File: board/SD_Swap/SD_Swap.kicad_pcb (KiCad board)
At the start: 4 copper layers, 32 x 27 mm, 44 parts, among them J1 USB_C, Q1 Q_Dual_PNP_PNP_E1B1C2E2B2C1, U1 74LVC2G14, U2 RTS5306E, U3 PCB_SD, U4 93AAxxAT, U5 TS3A27518ERTW, U6 SD_SOCKET, U7 AP2127N-3.3, Y1 12MHz

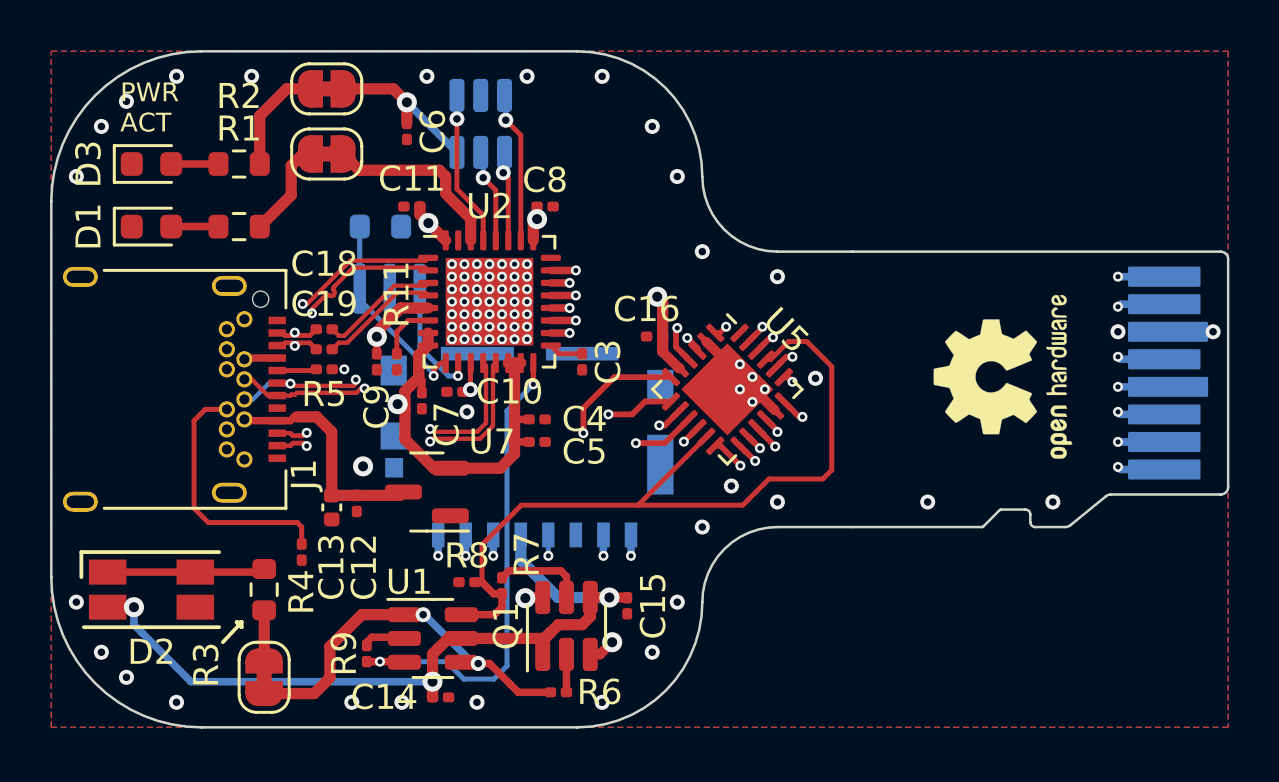
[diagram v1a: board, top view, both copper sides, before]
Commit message: update fix led
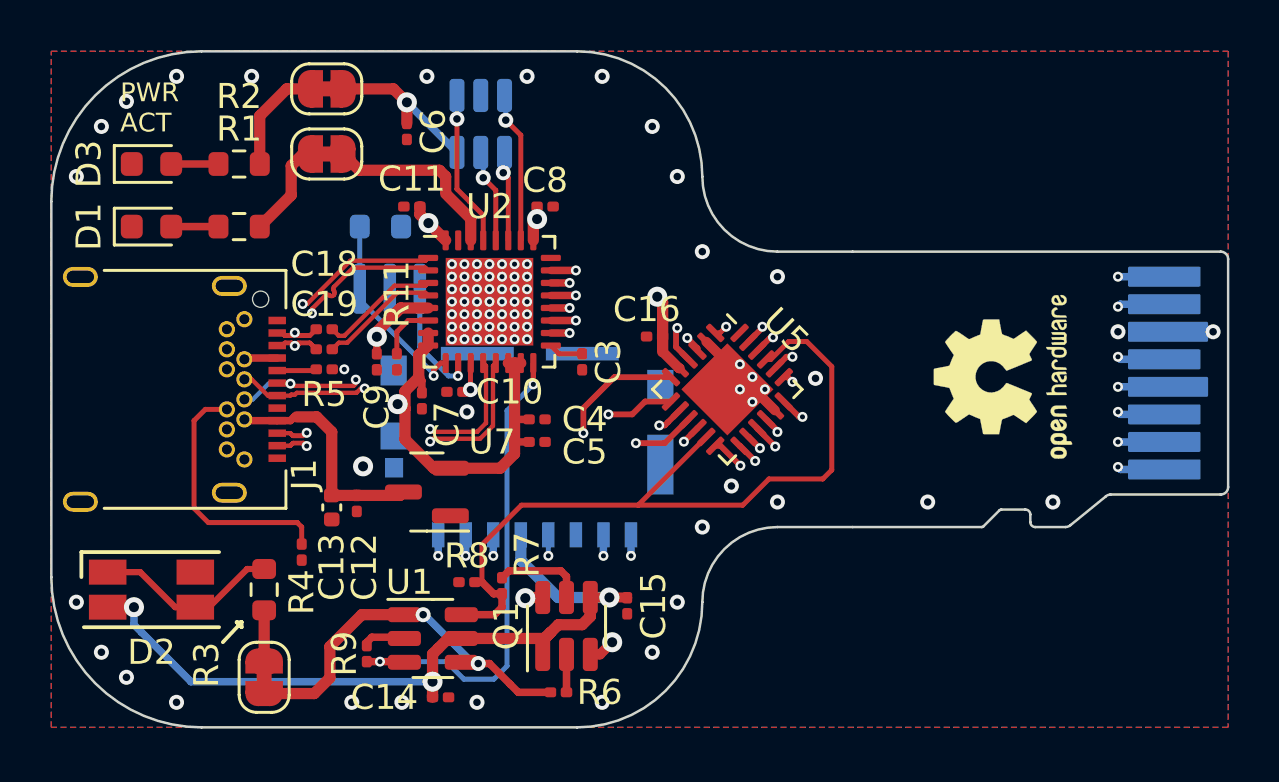
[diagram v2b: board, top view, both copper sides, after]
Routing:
- net Net-(D2-Pad1): track 6.30 -> 7.64 mm
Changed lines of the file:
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@@
     (pad "2" smd rect (at -1.75 0.7 180) (size 1.5 1) (layers "F.Cu" "F.Paste" "F.Mask")
       (net 13 "VCC") (pinfunction "A2") (pintype "input"))
-    (pad "3" smd rect (at 1.75 0.7 180) (size 1.5 1) (layers "F.Cu" "F.Paste" "F.Mask")
+    (pad "3" smd rect (at 1.75 -0.7 180) (size 1.5 1) (layers "F.Cu" "F.Paste" "F.Mask")
       (net 1 "GND") (pinfunction "K1") (pintype "input"))
-    (pad "4" smd rect (at 1.75 -0.7 180) (size 1.5 1) (layers "F.Cu" "F.Paste" "F.Mask")
+    (pad "4" smd rect (at 1.75 0.7 180) (size 1.5 1) (layers "F.Cu" "F.Paste" "F.Mask")
       (net 14 "Net-(D2-Pad1)") (pinfunction "K2") (pintype "input"))
     (model "${KICAD6_3DMODEL_DIR}/LED_SMD.3dshapes/LED_RGB_1210.wrl"
@@
     (fp_line (start 6.9 10.3) (end 5.94 10.3) (layer "Edge.Cuts") (width 0.1))
     (fp_line (start 10.11 9.78) (end 8.71 10.919641) (layer "Edge.Cuts") (width 0.1))
-    (fp_arc (start 10.11 9.78) (mid 10.198119 9.723665) (end 10.3 9.7) (layer "Edge.Cuts") (width 0.1))
-    (fp_arc (start 5.23 10.971005) (mid 5.197895 10.992494) (end 5.160001 11) (layer "Edge.Cuts") (width 0.1))
-    (fp_arc (start 5.870001 10.328995) (mid 5.902112 10.307528) (end 5.94 10.3) (layer "Edge.Cuts") (width 0.1))
+    (fp_arc (start 10.11 9.78) (mid 10.198122 9.723662) (end 10.3 9.7) (layer "Edge.Cuts") (width 0.1))
+    (fp_arc (start 5.23 10.971005) (mid 5.197895 10.992482) (end 5.160001 11) (layer "Edge.Cuts") (width 0.1))
+    (fp_arc (start 5.870001 10.328995) (mid 5.902112 10.307516) (end 5.94 10.3) (layer "Edge.Cuts") (width 0.1))
     (fp_arc (start 6.9 10.3) (mid 7.041421 10.358579) (end 7.1 10.5) (layer "Edge.Cuts") (width 0.1))
     (fp_arc (start 7.3 11) (mid 7.158579 10.941421) (end 7.1 10.8) (layer "Edge.Cuts") (width 0.1))
@@
   (segment (start 96.575 93.175) (end 106.225 93.175) (width 0.3) (layer "B.Cu") (net 13))
   (segment (start 94.3 90.2) (end 94.3 90.9) (width 0.3) (layer "B.Cu") (net 13))
+  (segment (start 93.25 88.8) (end 94.55 88.8) (width 0.25) (layer "F.Cu") (net 14))
+  (segment (start 95.95 90.2) (end 96.75 90.2) (width 0.25) (layer "F.Cu") (net 14))
+  (segment (start 98.825 88.675) (end 99.5 88.675) (width 0.25) (layer "F.Cu") (net 14))
+  (segment (start 97.3 90.2) (end 98.825 88.675) (width 0.25) (layer "F.Cu") (net 14))
   (segment (start 99.375 88.8) (end 99.5 88.675) (width 0.3) (layer "F.Cu") (net 14))
-  (segment (start 96.75 88.8) (end 99.375 88.8) (width 0.3) (layer "F.Cu") (net 14))
-  (segment (start 93.25 88.8) (end 96.75 88.8) (width 0.3) (layer "F.Cu") (net 14))
+  (segment (start 94.55 88.8) (end 95.95 90.2) (width 0.25) (layer "F.Cu") (net 14))
+  (segment (start 96.75 90.2) (end 97.3 90.2) (width 0.25) (layer "F.Cu") (net 14))
   (segment (start 96.7 82.75) (end 96.7 86.25) (width 0.2) (layer "F.Cu") (net 15))
   (segment (start 97.27 86.82) (end 100.82 86.82) (width 0.2) (layer "F.Cu") (net 15))

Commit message: fixed clearance issue pnp base resistor is now 100R
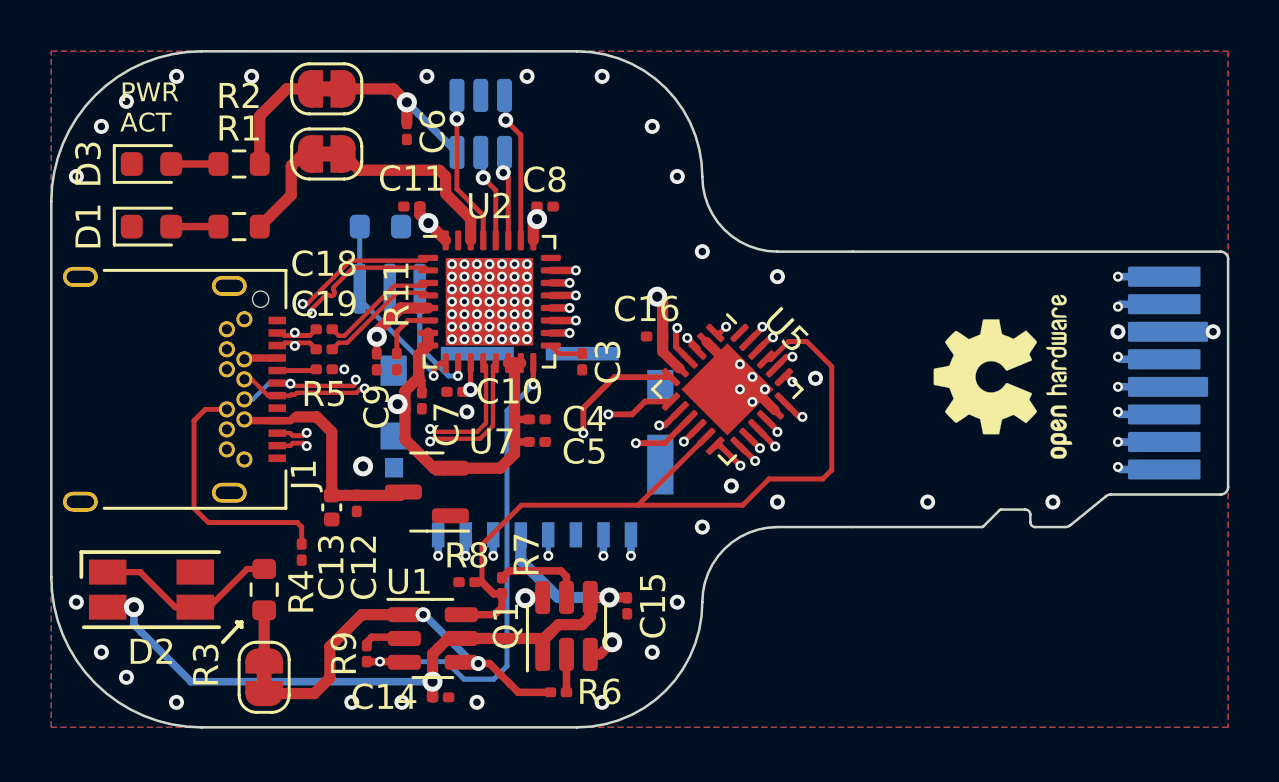
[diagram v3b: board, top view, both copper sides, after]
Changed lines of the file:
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@@
     (fp_line (start 6.9 10.3) (end 5.94 10.3) (layer "Edge.Cuts") (width 0.1))
     (fp_line (start 10.11 9.78) (end 8.71 10.919641) (layer "Edge.Cuts") (width 0.1))
-    (fp_arc (start 10.11 9.78) (mid 10.198122 9.723662) (end 10.3 9.7) (layer "Edge.Cuts") (width 0.1))
-    (fp_arc (start 5.23 10.971005) (mid 5.197895 10.992482) (end 5.160001 11) (layer "Edge.Cuts") (width 0.1))
-    (fp_arc (start 5.870001 10.328995) (mid 5.902112 10.307516) (end 5.94 10.3) (layer "Edge.Cuts") (width 0.1))
+    (fp_arc (start 10.11 9.78) (mid 10.198117 9.723644) (end 10.3 9.7) (layer "Edge.Cuts") (width 0.1))
+    (fp_arc (start 5.23 10.971005) (mid 5.197895 10.992494) (end 5.160001 11) (layer "Edge.Cuts") (width 0.1))
+    (fp_arc (start 5.870001 10.328995) (mid 5.902112 10.307528) (end 5.94 10.3) (layer "Edge.Cuts") (width 0.1))
     (fp_arc (start 6.9 10.3) (mid 7.041421 10.358579) (end 7.1 10.5) (layer "Edge.Cuts") (width 0.1))
     (fp_arc (start 7.3 11) (mid 7.158579 10.941421) (end 7.1 10.8) (layer "Edge.Cuts") (width 0.1))
@@
   (segment (start 96.575 93.175) (end 106.225 93.175) (width 0.3) (layer "B.Cu") (net 13))
   (segment (start 94.3 90.2) (end 94.3 90.9) (width 0.3) (layer "B.Cu") (net 13))
+  (segment (start 99.5 88.675) (end 98.825 88.675) (width 0.25) (layer "F.Cu") (net 14))
+  (segment (start 98.825 88.675) (end 97.3 90.2) (width 0.25) (layer "F.Cu") (net 14))
   (segment (start 93.25 88.8) (end 94.55 88.8) (width 0.25) (layer "F.Cu") (net 14))
   (segment (start 95.95 90.2) (end 96.75 90.2) (width 0.25) (layer "F.Cu") (net 14))
-  (segment (start 98.825 88.675) (end 99.5 88.675) (width 0.25) (layer "F.Cu") (net 14))
-  (segment (start 97.3 90.2) (end 98.825 88.675) (width 0.25) (layer "F.Cu") (net 14))
-  (segment (start 99.375 88.8) (end 99.5 88.675) (width 0.3) (layer "F.Cu") (net 14))
   (segment (start 94.55 88.8) (end 95.95 90.2) (width 0.25) (layer "F.Cu") (net 14))
-  (segment (start 96.75 90.2) (end 97.3 90.2) (width 0.25) (layer "F.Cu") (net 14))
+  (segment (start 97.3 90.2) (end 96.75 90.2) (width 0.25) (layer "F.Cu") (net 14))
   (segment (start 96.7 82.75) (end 96.7 86.25) (width 0.2) (layer "F.Cu") (net 15))
   (segment (start 97.27 86.82) (end 100.82 86.82) (width 0.2) (layer "F.Cu") (net 15))
@@
   (segment (start 106.75 80.45) (end 106.55 80.45) (width 0.2) (layer "F.Cu") (net 56))
   (via (at 106.27 80.96) (size 0.4) (drill 0.2) (layers "F.Cu" "B.Cu") (net 56))
+  (segment (start 106.27 80.96) (end 106.27 80.849756) (width 0.2) (layer "B.Cu") (net 56))
+  (segment (start 103.317501 77.897257) (end 103.317501 77.4825) (width 0.2) (layer "B.Cu") (net 56))
   (segment (start 103.32 75) (end 103.317501 75.002499) (width 0.2) (layer "B.Cu") (net 56))
-  (segment (start 106.27 80.875211) (end 103.317501 77.922712) (width 0.2) (layer "B.Cu") (net 56))
-  (segment (start 106.27 80.96) (end 106.27 80.875211) (width 0.2) (layer "B.Cu") (net 56))
   (segment (start 103.317501 75.002499) (end 103.317501 77.4825) (width 0.2) (layer "B.Cu") (net 56))
-  (segment (start 103.317501 77.922712) (end 103.317501 77.4825) (width 0.2) (layer "B.Cu") (net 56))
+  (segment (start 106.27 80.849756) (end 103.317501 77.897257) (width 0.2) (layer "B.Cu") (net 56))
   (segment (start 107.25 80.953632) (end 107.239333 80.964299) (width 0.2) (layer "F.Cu") (net 57))
   (segment (start 107.25 80.45) (end 107.25 80.953632) (width 0.2) (layer "F.Cu") (net 57))

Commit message: update PCB to fix USB3 issues
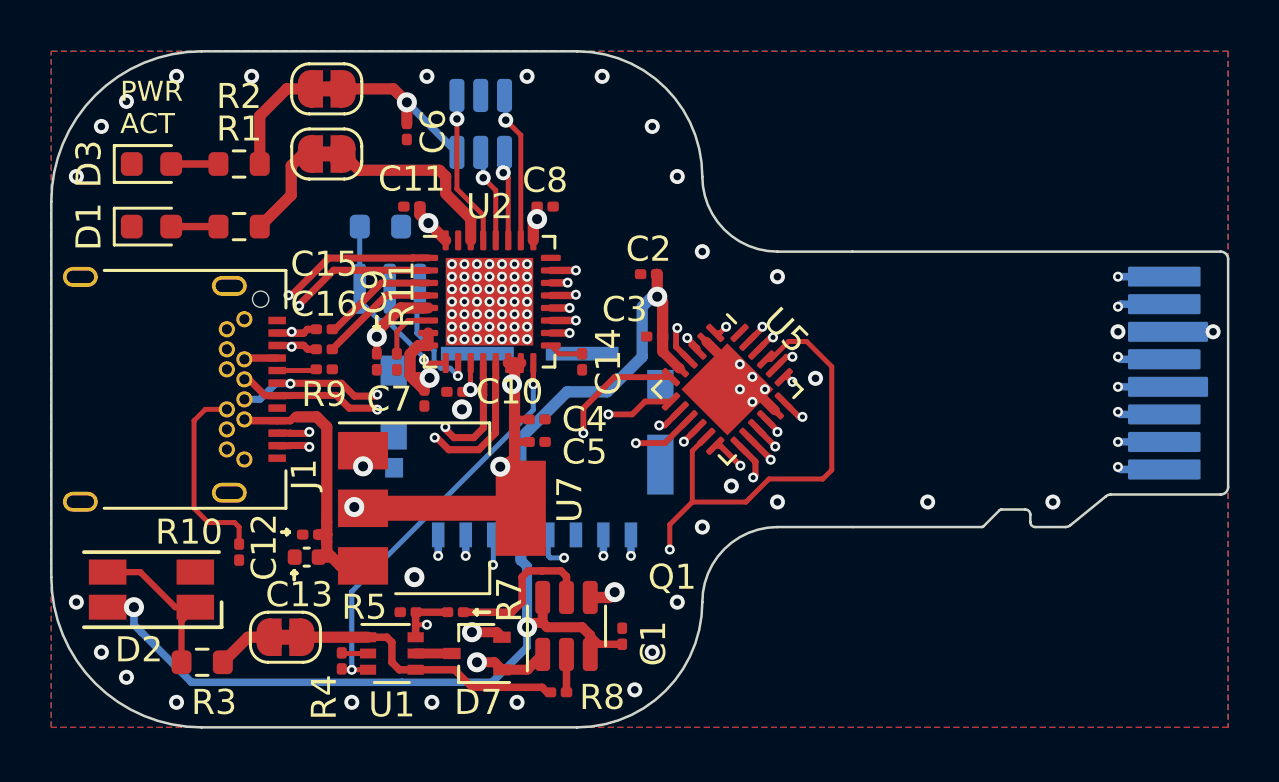
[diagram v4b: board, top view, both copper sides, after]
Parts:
- removed REF**: OSHW-Logo2_7.3x6mm_SilkScreen, Symbol:OSHW-Logo2_7.3x6mm_SilkScreen
- added D7: BAT54CW, Package_TO_SOT_SMD:SOT-323_SC-70, F.Cu at (108.0, 92.0)
- R4: renamed from R9; value 6.2k -> 6.2K
- R5: renamed from R8; value 6.2k -> 6.2K
- R7: value 1K -> 100
- R8: renamed from R6; value 1K -> 100
- U1: footprint Package_TO_SOT_SMD:SOT-23-6 -> Package_TO_SOT_SMD:SOT-363_SC-70-6
- U7: value AP2127N-3.3 -> AZ1117-3.3; footprint Package_TO_SOT_SMD:SOT-23 -> Package_TO_SOT_SMD:SOT-223-3_TabPin2
- moved C2 13.3 mm to (114.9, 76.9), turned to 180 degrees
- moved C1 7.65 mm to (113.8, 91.4), turned to 90 degrees
- moved R3 3.81 mm to (97.0, 92.4), turned to 180 degrees
- moved R5 2.63 mm to (105.3, 90.4)
- moved R10 2.50 mm to (98.5, 88.0)
- moved C13 2.22 mm to (101.2, 88.2), turned to 180 degrees
- moved C12 2.22 mm to (101.4, 87.3), turned to 180 degrees
- moved R7 2.13 mm to (107.1, 90.4), turned to 180 degrees
- moved JP3 1.81 mm to (100.3, 91.4), turned to 0 degrees
- moved U1 1.74 mm to (104.6, 92.0)
- moved R4 1.04 mm to (102.6, 92.3)
- moved U7 0.88 mm to (106.6, 86.2), turned to 0 degrees
- moved C7 0.15 mm to (105.9, 81.8)
- turned D2 to 180 degrees
- renumbered C14 to C1, C3 to C14, C18 to C15, C19 to C16, C15 to C2, C16 to C3, R4 to R10, R10 to R6, R5 to R9
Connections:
- D2 pad 1: Net-(D2-Pad1) -> Net-(D2-A1)
- D2 pad 4: Net-(D2-Pad1) -> Net-(D2-A1)
- JP3 pad 1: Net-(JP3-Pad1) -> Net-(JP3-A)
- Q1 pad 1: VCC -> +3.3V
- Q1 pad 3: Net-(Q1-Pad3) -> VCC
- Q1 pad 4: VCC -> /SD_VCC
- Q1 pad 6: +3.3V -> VCC
- R3 pad 1: Net-(D2-Pad1) -> Net-(JP3-A)
- R3 pad 2: Net-(JP3-Pad1) -> Net-(D2-A1)
- U1 pad 5: VCC -> /INV_PWR
- U3 pad 4: Net-(Q1-Pad3) -> /SD_VCC
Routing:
- net +3.3V: track 49.3 -> 28.8 mm, vias 3 -> 6
- net VCC: track 35.4 -> 46.6 mm, vias 4 -> 3
- net Net-(D2-Pad1): track 7.46 -> 0.00 mm
- net Net-(D2-A1): track 0.00 -> 6.51 mm
- net /SD_VCC: track 0.00 -> 4.35 mm, vias 0 -> 3
- net Net-(JP3-B): track 15.5 -> 11.3 mm, vias 2 -> 0
- net Net-(U2-CARD_3V3): track 20.3 -> 17.0 mm
- net /USB-: track 14.6 -> 17.7 mm
- net Net-(Q1-Pad3): track 3.08 -> 0.00 mm, vias 2 -> 0
- net Net-(Q1B-B2): track 3.62 -> 6.31 mm
- net /USB+: track 16.4 -> 19.0 mm
- net Net-(J1-CC2): track 10.3 -> 7.79 mm
- net Net-(JP3-A): track 0.00 -> 2.26 mm
- net /SS_RX+: track 19.0 -> 21.2 mm
- net /SS_RX-: track 19.0 -> 21.1 mm
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- added copper zone on In1.Cu, net +3.3V
- added copper zone on In2.Cu, net /SD_VCC
- removed copper zone on In1.Cu, net Net-(Q1-Pad3)
- removed copper zone on In2.Cu, net VCC
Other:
- rule pad_to_mask_clearance: 0 -> 0.038
